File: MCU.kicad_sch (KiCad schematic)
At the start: 6 parts, among them U1 STM32H745ZITx

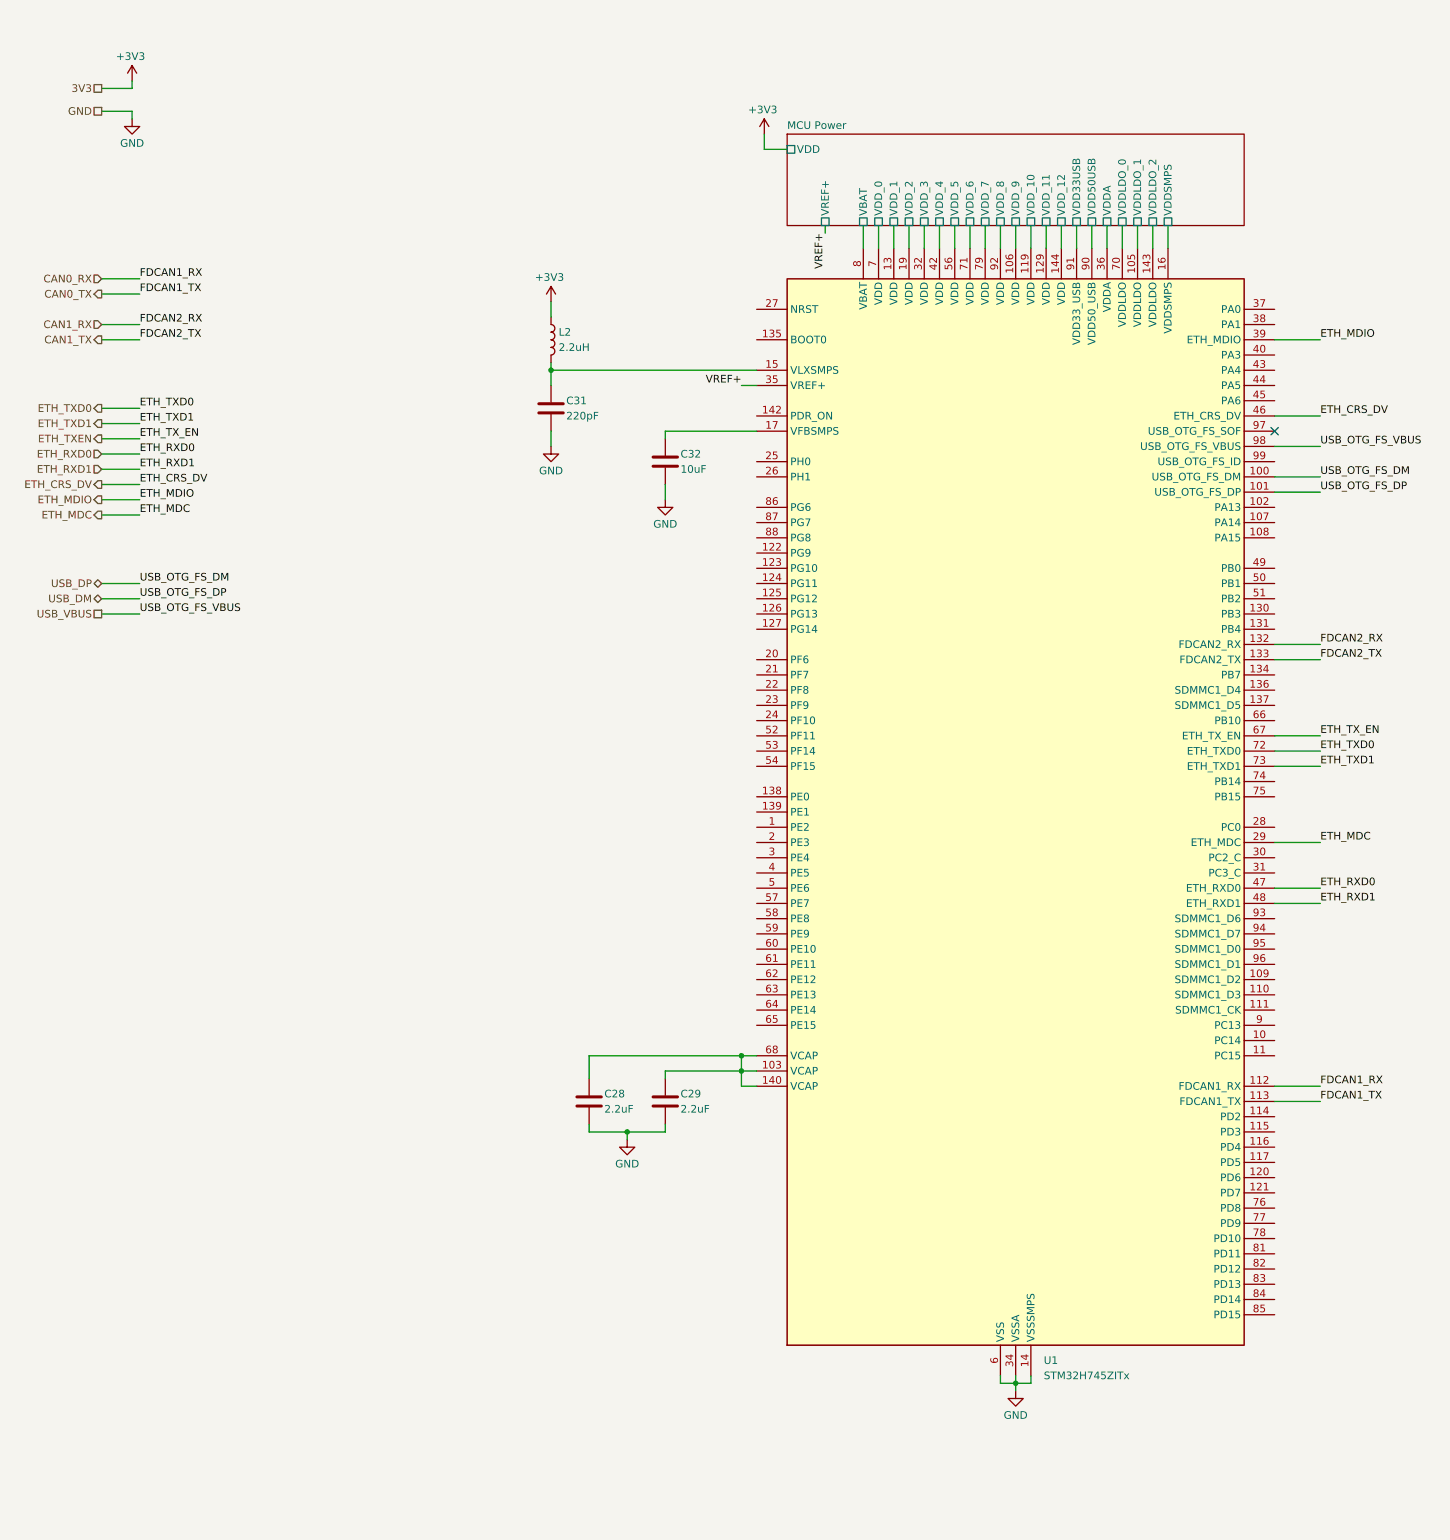
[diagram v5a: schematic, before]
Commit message: routed more sheets, improved analogs. next 5v /analog ground
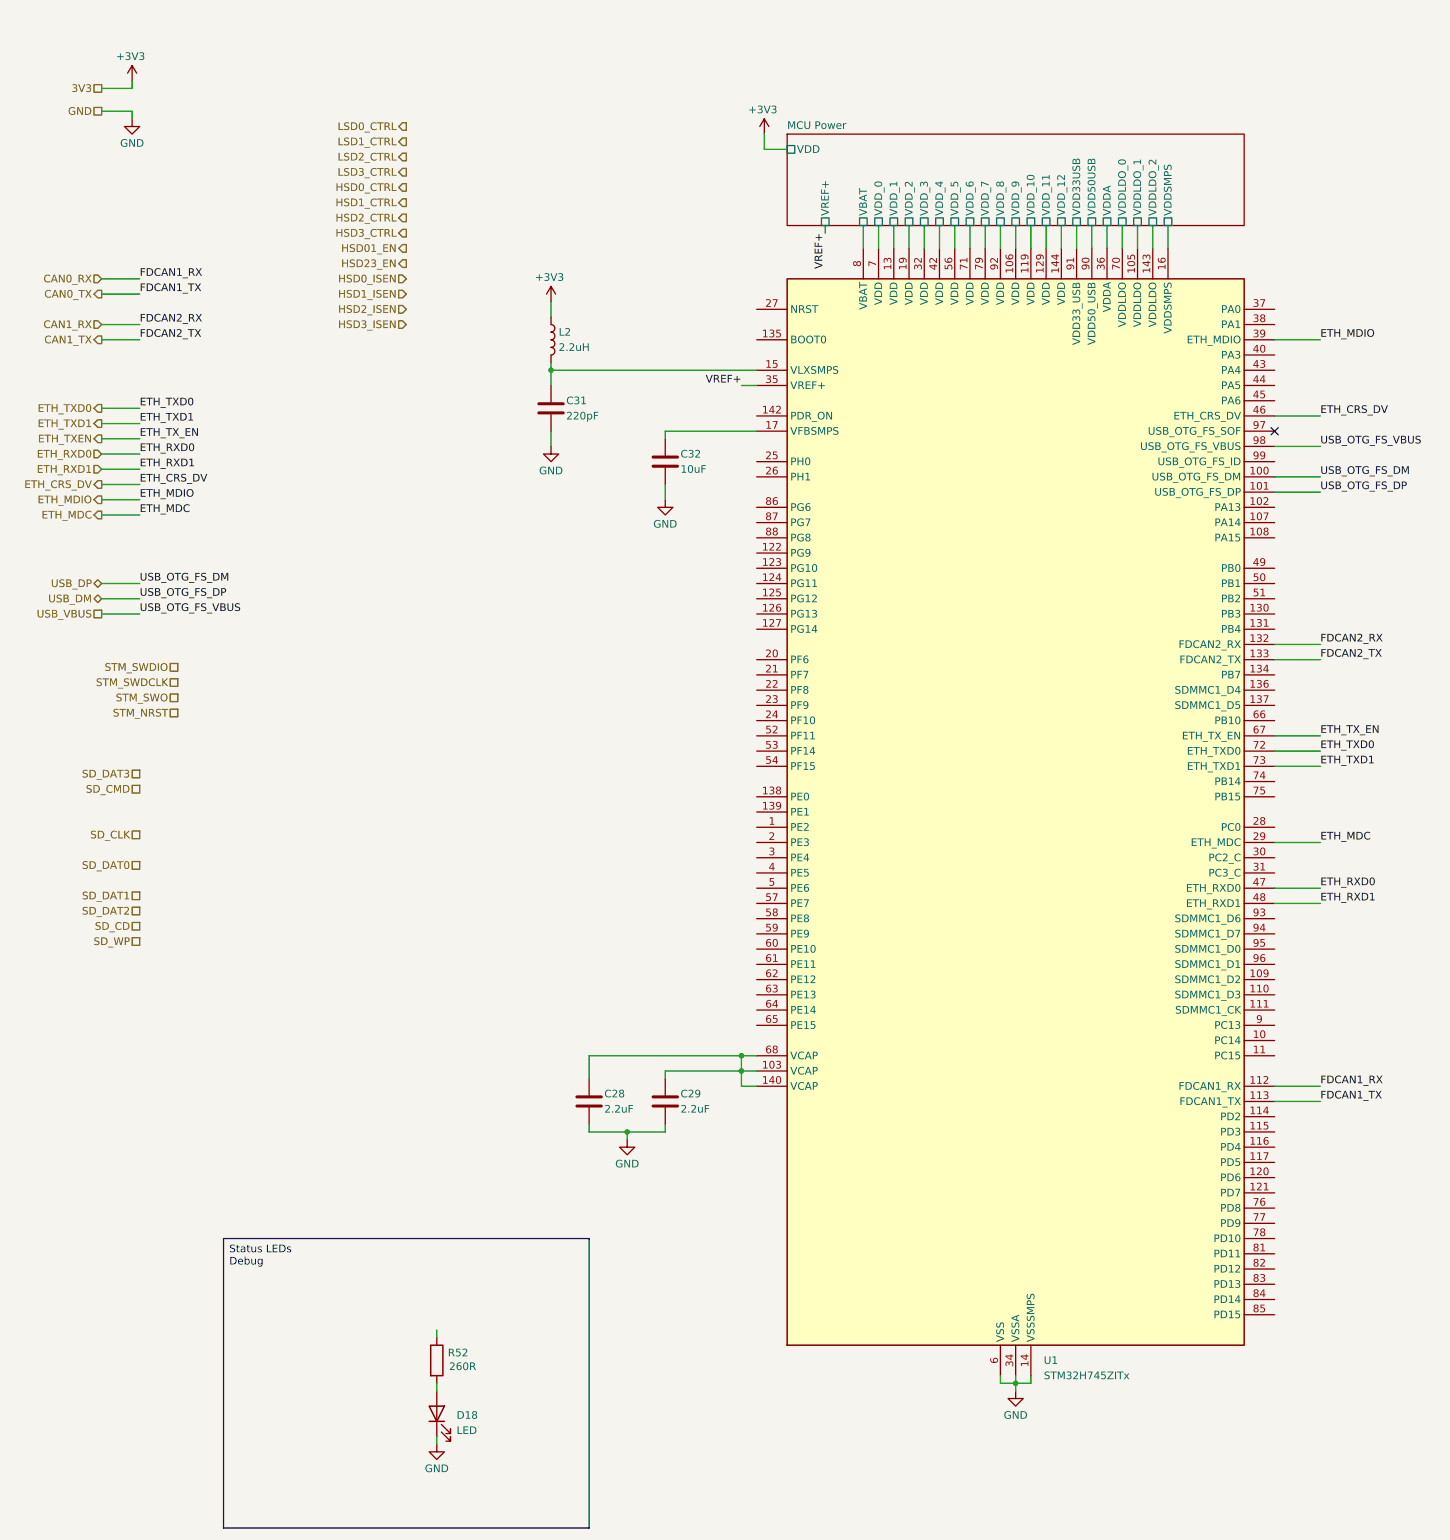
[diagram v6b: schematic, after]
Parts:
- added D18: LED, LED_SMD:LED_0603_1608Metric_Pad1.05x0.95mm_HandSolder, symbol Device:LED
- added R52: 260R, Resistor_SMD:R_0603_1608Metric_Pad0.98x0.95mm_HandSolder, symbol Device:R
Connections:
- net GND: now also D18.1 (K)
- new net: D18.2 (A), R52.2

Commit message: improved analogs
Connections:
- net GND: no longer U1.34 (VSSA)
- net +3V3 renamed 3V3
- new net AGND: U1.34 (VSSA)
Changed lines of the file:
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@@
-	)
-	(junction
-		(at 177.8 247.65)
-		(diameter 0)
-		(color 0 0 0 0)
 	)
 	(junction
@@
 		(color 0 0 0 0)
 	)
+	(junction
+		(at 175.26 250.19)
+		(diameter 0)
+		(color 0 0 0 0)
+	)
 	(no_connect
 		(at 220.98 88.9)
@@
 	(wire
 		(pts
+			(xy 30.48 44.45) (xy 30.48 43.18)
+		)
+		(stroke
+			(width 0)
+			(type default)
+		)
+	)
+	(wire
+		(pts
+			(xy 177.8 246.38) (xy 177.8 252.73)
+		)
+		(stroke
+			(width 0)
+			(type default)
+		)
+	)
+	(wire
+		(pts
+			(xy 170.18 250.19) (xy 175.26 250.19)
+		)
+		(stroke
+			(width 0)
+			(type default)
+		)
+	)
+	(wire
+		(pts
 			(xy 25.4 31.75) (xy 30.48 31.75)
 		)
@@
 	(wire
 		(pts
-			(xy 180.34 246.38) (xy 180.34 247.65)
+			(xy 180.34 246.38) (xy 180.34 250.19)
+		)
+		(stroke
+			(width 0)
+			(type default)
+		)
+	)
+	(wire
+		(pts
+			(xy 30.48 43.18) (xy 25.4 43.18)
 		)
 		(stroke
@@
 	(wire
 		(pts
-			(xy 177.8 247.65) (xy 180.34 247.65)
+			(xy 175.26 250.19) (xy 180.34 250.19)
 		)
 		(stroke
@@
 	(wire
 		(pts
+			(xy 170.18 250.19) (xy 170.18 252.73)
+		)
+		(stroke
+			(width 0)
+			(type default)
+		)
+	)
+	(wire
+		(pts
 			(xy 134.62 198.12) (xy 132.08 198.12)
 		)
@@
 	(wire
 		(pts
-			(xy 177.8 247.65) (xy 177.8 248.92)
-		)
-		(stroke
-			(width 0)
-			(type default)
-		)
-	)
-	(wire
-		(pts
-			(xy 177.8 246.38) (xy 177.8 247.65)
-		)
-		(stroke
-			(width 0)
-			(type default)
-		)
-	)
-	(wire
-		(pts
 			(xy 119.38 88.9) (xy 134.62 88.9)
 		)
@@
 	(wire
 		(pts
-			(xy 175.26 247.65) (xy 177.8 247.65)
-		)
-		(stroke
-			(width 0)
-			(type default)
-		)
-	)
-	(wire
-		(pts
 			(xy 106.68 193.04) (xy 106.68 196.85)
 		)
@@
 	(wire
 		(pts
+			(xy 175.26 246.38) (xy 175.26 250.19)
+		)
+		(stroke
+			(width 0)
+			(type default)
+		)
+	)
+	(wire
+		(pts
 			(xy 228.6 142.24) (xy 220.98 142.24)
-		)
-		(stroke
-			(width 0)
-			(type default)
-		)
-	)
-	(wire
-		(pts
-			(xy 175.26 246.38) (xy 175.26 247.65)
 		)
 		(stroke
@@
 		(shape output)
 		(at 25.4 87.63 180)
+		(effects
+			(font
+				(size 1.27 1.27)
+			)
+			(justify right)
+		)
+	)
+	(hierarchical_label "AGND"
+		(shape passive)
+		(at 25.4 43.18 180)
 		(effects
 			(font
@@
 	(symbol
 		(lib_id "power:GND")
-		(at 177.8 248.92 0)
+		(at 170.18 252.73 0)
 		(unit 1)
 		(exclude_from_sim no)
@@
 		(dnp no)
 		(property "Reference" "#PWR037"
-			(at 177.8 255.27 0)
+			(at 170.18 259.08 0)
 			(effects
 				(font
@@
 		)
 		(property "Value" "GND"
-			(at 177.8 252.984 0)
+			(at 170.18 256.794 0)
 			(effects
 				(font
@@
 		)
 		(property "Footprint" ""
-			(at 177.8 248.92 0)
+			(at 170.18 252.73 0)
 			(effects
 				(font
@@
 		)
 		(property "Datasheet" ""
-			(at 177.8 248.92 0)
+			(at 170.18 252.73 0)
 			(effects
 				(font
@@
 		)
 		(property "Description" "Power symbol creates a global label with name \"GND\" , ground"
-			(at 177.8 248.92 0)
+			(at 170.18 252.73 0)
 			(effects
 				(font
@@
 			)
 		)
-		(property "Value" "+3V3"
+		(property "Value" "3V3"
 			(at 135.636 35.306 0)
 			(effects
@@
 			)
 		)
-		(property "Value" "+3V3"
+		(property "Value" "3V3"
 			(at 100.076 63.246 0)
 			(effects
@@
 	)
 	(symbol
+		(lib_id "power:GND")
+		(at 177.8 252.73 0)
+		(unit 1)
+		(exclude_from_sim no)
+		(in_bom yes)
+		(on_board yes)
+		(dnp no)
+		(property "Reference" "#PWR0181"
+			(at 177.8 259.08 0)
+			(effects
+				(font
+					(size 1.27 1.27)
+				)
+				(hide yes)
+			)
+		)
+		(property "Value" "AGND"
+			(at 177.8 256.794 0)
+			(effects
+				(font
+					(size 1.27 1.27)
+				)
+			)
+		)
+		(property "Footprint" ""
+			(at 177.8 252.73 0)
+			(effects
+				(font
+					(size 1.27 1.27)
+				)
+				(hide yes)
+			)
+		)
+		(property "Datasheet" ""
+			(at 177.8 252.73 0)
+			(effects
+				(font
+					(size 1.27 1.27)
+				)
+				(hide yes)
+			)
+		)
+		(property "Description" "Power symbol creates a global label with name \"GND\" , ground"
+			(at 177.8 252.73 0)
+			(effects
+				(font
+					(size 1.27 1.27)
+				)
+				(hide yes)
+			)
+		)
+		(pin "1"
+		)
+		(instances
+			(project "NCU"
+				(path "/3aee14c3-5480-4f7c-989e-3fef81779034/d2b1e1a0-8b64-49ff-b975-b40fa2d33dc6"
+					(reference "#PWR0181")
+					(unit 1)
+				)
+			)
+		)
+	)
+	(symbol
 		(lib_id "power:+5V")
 		(at 30.48 30.48 0)
@@
 			)
 		)
-		(property "Value" "+3V3"
+		(property "Value" "3V3"
 			(at 30.226 26.416 0)
 			(effects
@@
 					(unit 1)
 				)
+			)
+		)
+	)
+	(symbol
+		(lib_id "power:GND")
+		(at 30.48 44.45 0)
+		(unit 1)
+		(exclude_from_sim no)
+		(in_bom yes)
+		(on_board yes)
+		(dnp no)
+		(property "Reference" "#PWR0182"
+			(at 30.48 50.8 0)
+			(effects
+				(font
+					(size 1.27 1.27)
+				)
+				(hide yes)
+			)
+		)
+		(property "Value" "AGND"
+			(at 30.48 48.514 0)
+			(effects
+				(font
+					(size 1.27 1.27)
+				)
+			)
+		)
+		(property "Footprint" ""
+			(at 30.48 44.45 0)
+			(effects
+				(font
+					(size 1.27 1.27)
+				)
+				(hide yes)
+			)
+		)
+		(property "Datasheet" ""
+			(at 30.48 44.45 0)
+			(effects
+				(font
+					(size 1.27 1.27)
+				)
+				(hide yes)
+			)
+		)
+		(property "Description" "Power symbol creates a global label with name \"GND\" , ground"
+			(at 30.48 44.45 0)
+			(effects
+				(font
+					(size 1.27 1.27)
+				)
+				(hide yes)
+			)
+		)
+		(pin "1"
+		)
+		(instances
+			(project "NCU"
+				(path "/3aee14c3-5480-4f7c-989e-3fef81779034/d2b1e1a0-8b64-49ff-b975-b40fa2d33dc6"
+					(reference "#PWR0182")
+					(unit 1)
+				)

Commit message: lsd circuit in place
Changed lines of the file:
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@@
 		)
 	)
-	(hierarchical_label "HSD0_ISEN"
-		(shape input)
+	(hierarchical_label "HSD01_ISEN"
+		(shape passive)
 		(at 76.2 63.5 180)
 		(effects
@@
 	)
 	(hierarchical_label "LSD2_CTRL"
-		(shape output)
+		(shape passive)
 		(at 76.2 43.18 180)
 		(effects
@@
 	)
 	(hierarchical_label "LSD3_CTRL"
-		(shape output)
+		(shape passive)
 		(at 76.2 45.72 180)
 		(effects
@@
 		(shape passive)
 		(at 31.75 146.05 180)
-		(effects
-			(font
-				(size 1.27 1.27)
-			)
-			(justify right)
-		)
-	)
-	(hierarchical_label "HSD2_ISEN"
-		(shape input)
-		(at 76.2 68.58 180)
 		(effects
 			(font
@@
 	)
 	(hierarchical_label "HSD1_CTRL"
-		(shape output)
+		(shape passive)
 		(at 76.2 50.8 180)
 		(effects
@@
 		)
 	)
-	(hierarchical_label "HSD3_ISEN"
-		(shape input)
-		(at 76.2 71.12 180)
-		(effects
-			(font
-				(size 1.27 1.27)
-			)
-			(justify right)
-		)
-	)
 	(hierarchical_label "HSD3_CTRL"
-		(shape output)
+		(shape passive)
 		(at 76.2 55.88 180)
 		(effects
@@
 	)
 	(hierarchical_label "HSD23_EN"
-		(shape output)
+		(shape passive)
 		(at 76.2 60.96 180)
 		(effects
@@
 		)
 	)
-	(hierarchical_label "HSD1_ISEN"
-		(shape input)
+	(hierarchical_label "HSD23_ISEN"
+		(shape passive)
 		(at 76.2 66.04 180)
 		(effects
@@
 	)
 	(hierarchical_label "LSD1_CTRL"
-		(shape output)
+		(shape passive)
 		(at 76.2 40.64 180)
 		(effects
@@
 	)
 	(hierarchical_label "LSD0_CTRL"
-		(shape output)
+		(shape passive)
 		(at 76.2 38.1 180)
 		(effects
@@
 	)
 	(hierarchical_label "HSD0_CTRL"
-		(shape output)
+		(shape passive)
 		(at 76.2 48.26 180)
 		(effects
@@
 	)
 	(hierarchical_label "HSD2_CTRL"
-		(shape output)
+		(shape passive)
 		(at 76.2 53.34 180)
 		(effects
@@
 	)
 	(hierarchical_label "HSD01_EN"
-		(shape output)
+		(shape passive)
 		(at 76.2 58.42 180)
 		(effects
